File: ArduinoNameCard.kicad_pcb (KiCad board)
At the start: 2 copper layers, 91 x 55 mm, 24 parts, among them J1 Conn_01x05, J2 Conn_01x04, J3 Conn_01x06, J4 Conn_01x08, J5 Conn_01x06, SW1 SW_Push

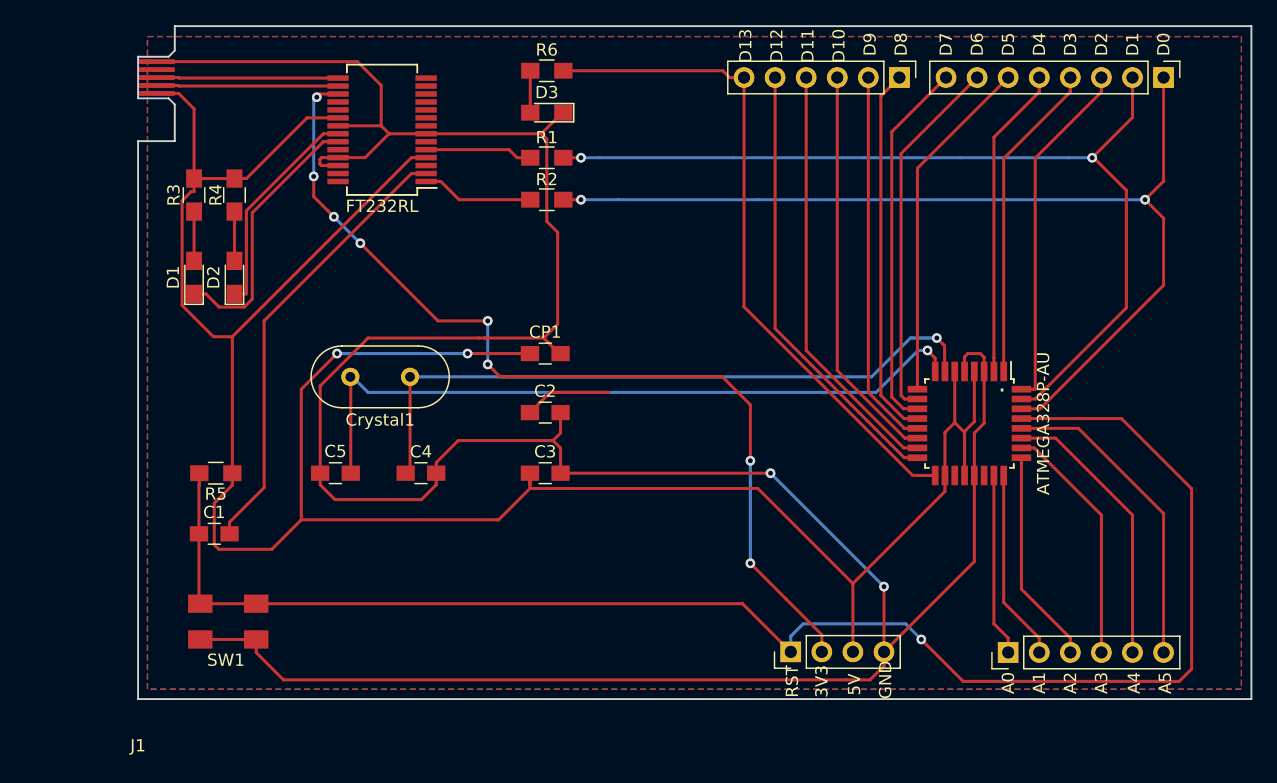
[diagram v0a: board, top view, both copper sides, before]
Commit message: ・READMEの更新 ・PCBの完成
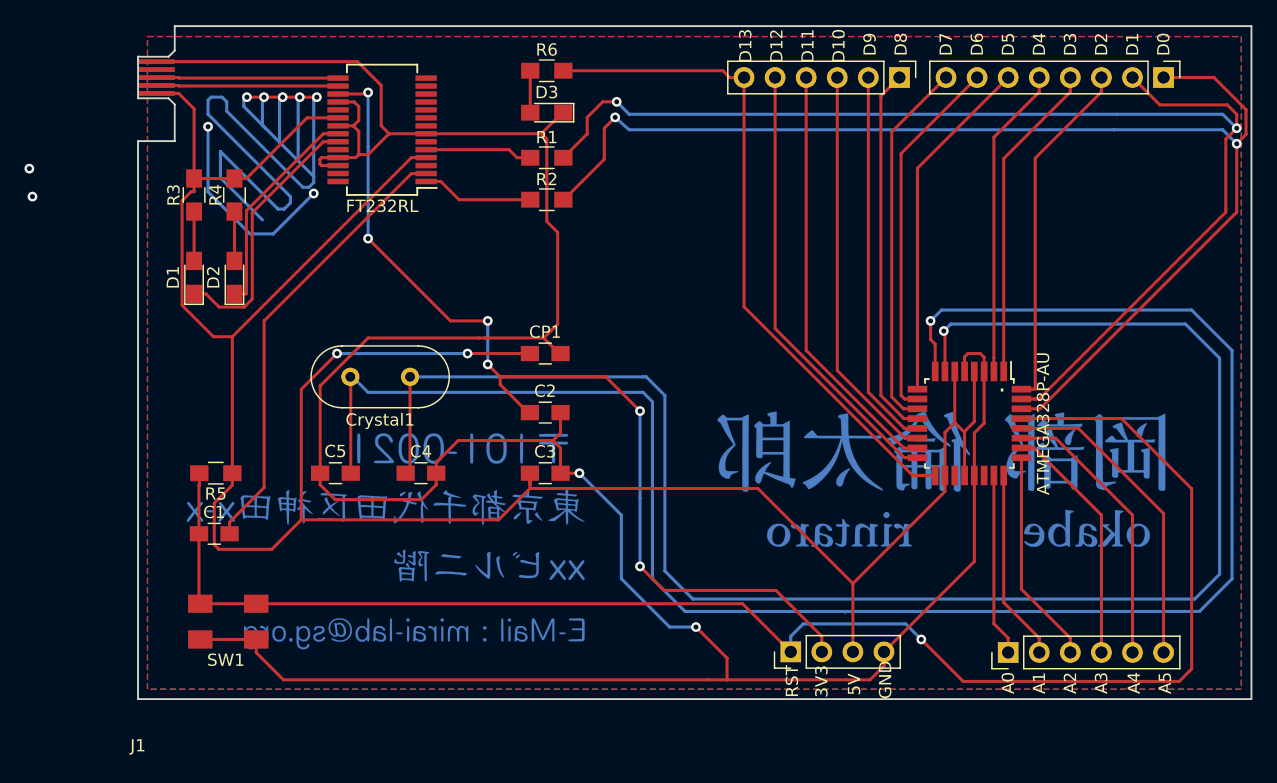
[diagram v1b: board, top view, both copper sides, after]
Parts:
- added G***: LOGO, ArduinoNameCard:belong_silk, B.Cu at (151.1, 77.0)
- added G***: LOGO, ArduinoNameCard:name_cu, B.Cu at (161.3, 99.7)
- added G***: LOGO, ArduinoNameCard:name_mask, B.Cu at (161.3, 99.7)
- added G***: LOGO, ArduinoNameCard:address_cu, B.Cu at (115.6, 104.4)
- added G***: LOGO, ArduinoNameCard:address_mask, B.Cu at (115.6, 104.4)
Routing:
- net (no net): track 0.00 -> 88.8 mm, vias 0 -> 9
- net Net-(C5-Pad1): track 59.3 -> 147.3 mm
- net Net-(C4-Pad1): track 55.4 -> 136.0 mm
- net RX: track 76.3 -> 100.0 mm
- net TX: track 81.6 -> 100.9 mm
- net GND: track 252.3 -> 245.3 mm
- net 3.3V: track 84.6 -> 79.8 mm, vias 8 -> 6

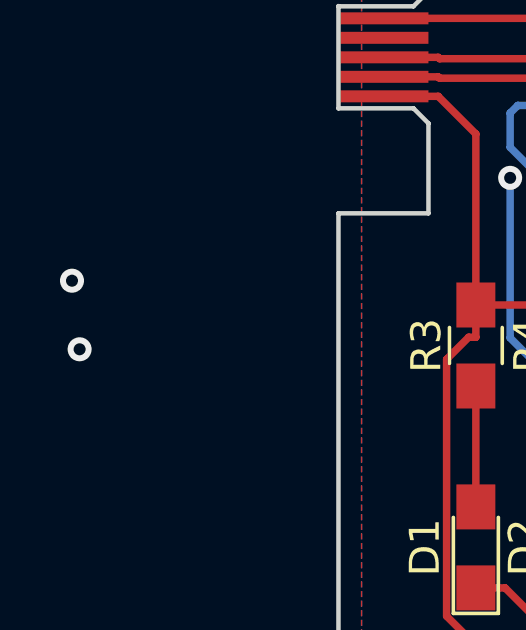
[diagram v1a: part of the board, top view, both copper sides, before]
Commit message: ・枠外にviaが残っていたので削除 ・回路図のpdfを追加
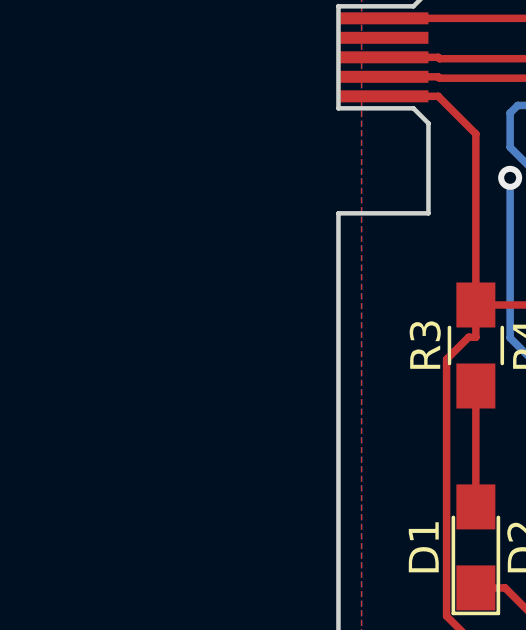
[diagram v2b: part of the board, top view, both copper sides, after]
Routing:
- net (no net): vias 9 -> 7
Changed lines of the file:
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@@
     (links 73)
     (no_connects 0)
-    (area 85.867999 61.21238 187.025001 121.645)
+    (area 91.002381 61.21238 187.025001 121.645)
     (thickness 1.6)
     (drawings 37)
-    (tracks 408)
+    (tracks 406)
     (zones 0)
     (modules 29)
@@
     (pcbplotparams
       (layerselection 0x010f0_80000001)
-      (usegerberextensions true)
+      (usegerberextensions false)
       (excludeedgelayer true)
       (linewidth 0.100000)
@@
       (plotinvisibletext false)
       (padsonsilk false)
-      (subtractmaskfromsilk true)
-      (outputformat 1)
+      (subtractmaskfromsilk false)
+      (outputformat 4)
       (mirror false)
       (drillshape 0)
@@
   (gr_line (start 95.75 64.25) (end 95.75 67.66) (angle 90) (layer Edge.Cuts) (width 0.15))
   (via (at 101.473 69.977) (size 0.8) (drill 0.4) (layers F.Cu B.Cu) (net 0))
-  (via (at 87.122 75.692) (size 0.8) (drill 0.4) (layers F.Cu B.Cu) (net 0))
-  (via (at 86.868 73.406) (size 0.8) (drill 0.4) (layers F.Cu B.Cu) (net 0))
   (via (at 110.109 75.438) (size 0.8) (drill 0.4) (layers F.Cu B.Cu) (net 0))
   (segment (start 101.473 69.977) (end 101.473 75.311) (width 0.25) (layer B.Cu) (net 0))

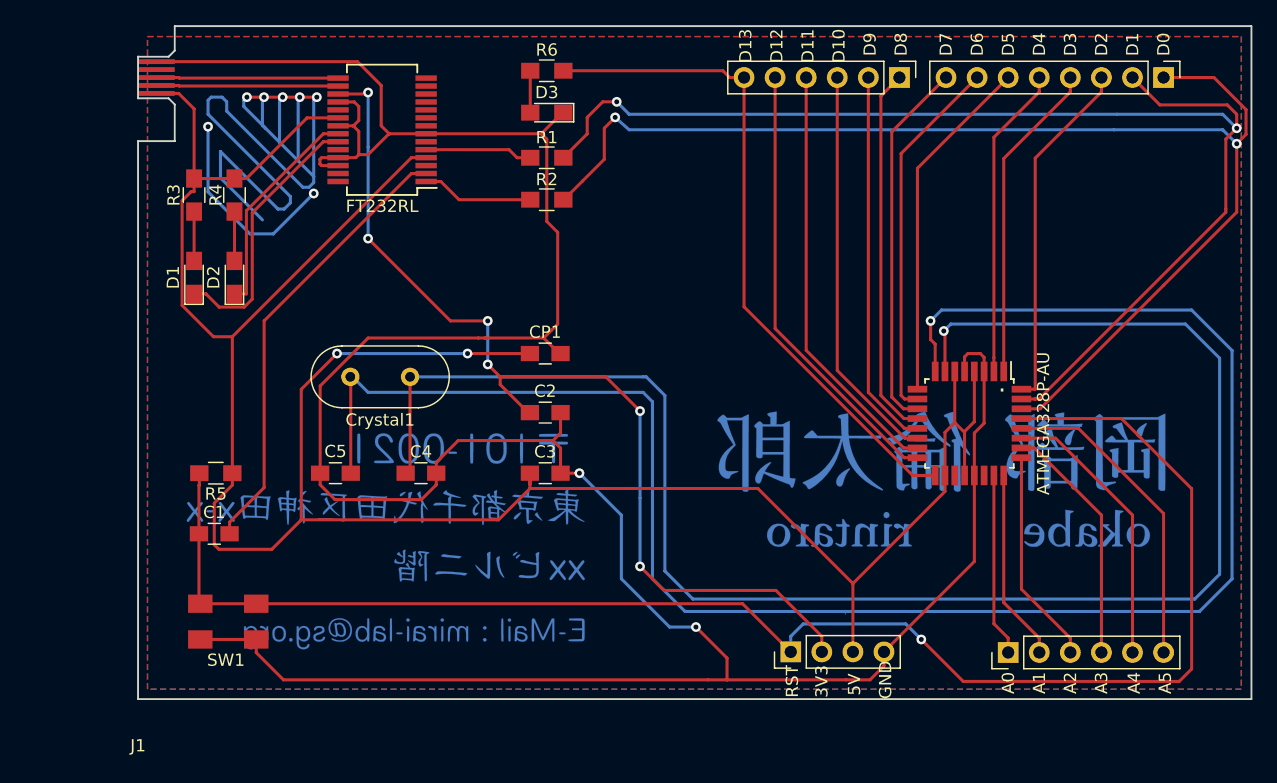
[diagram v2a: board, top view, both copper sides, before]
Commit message: 回路にヒューズを追加した
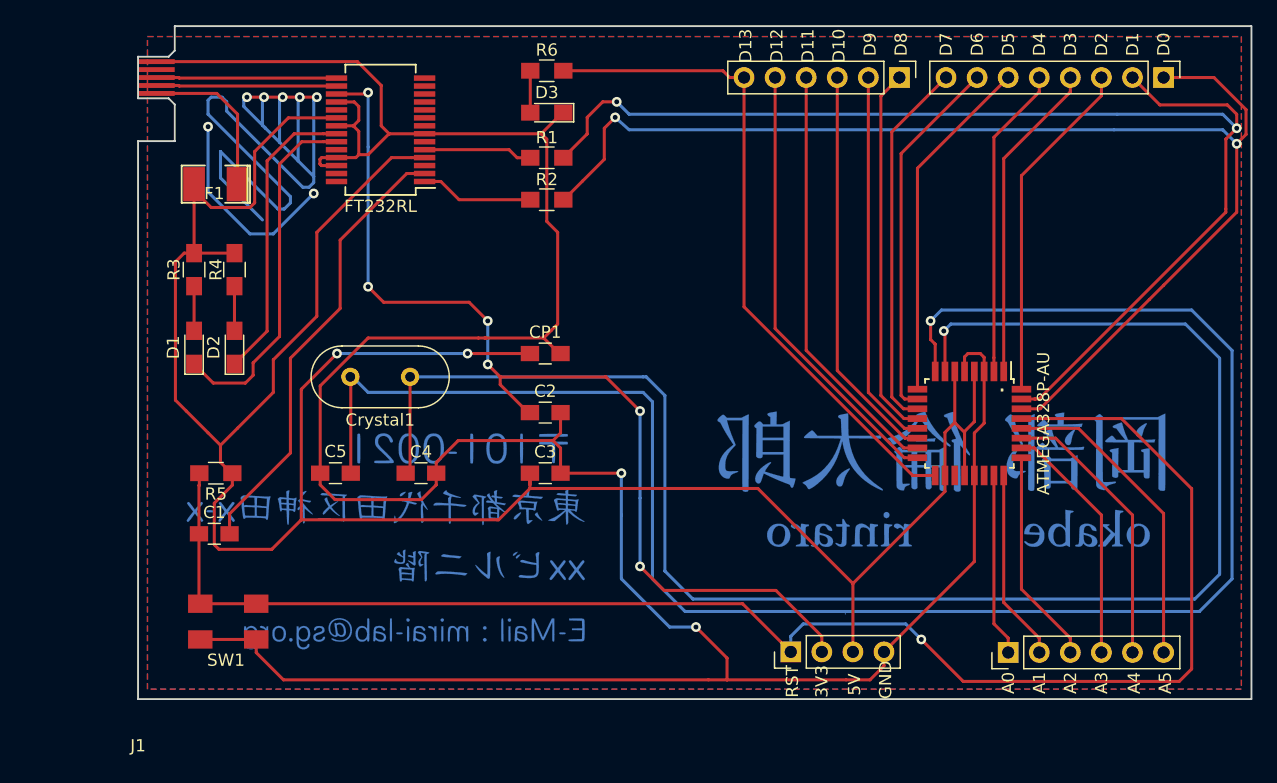
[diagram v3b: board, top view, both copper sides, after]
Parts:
- added F1: 500mA, SMD_Packages:SMD-1210_Pol, F.Cu at (102.1, 74.7)
- moved R3 6.10 mm to (100.3, 81.7)
- moved R4 6.10 mm to (103.6, 81.7)
- moved D1 5.71 mm to (100.3, 88.0)
- moved D2 5.71 mm to (103.6, 88.0)
- moved FT232RL 0.13 mm to (115.6, 70.2)
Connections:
- ATMEGA328P-AU pad 18: +5V -> 5V
- ATMEGA328P-AU pad 20: +5V -> 5V
- ATMEGA328P-AU pad 4: +5V -> 5V
- ATMEGA328P-AU pad 6: +5V -> 5V
- C3 pad 1: +5V -> 5V
- CP1 pad 1: +5V -> 5V
- FT232RL pad 20: +5V -> 5V
- FT232RL pad 4: +5V -> 5V
- J2 pad 3: +5V -> 5V
- R3 pad 1: +5V -> 5V
- R4 pad 1: +5V -> 5V
- R5 pad 1: +5V -> 5V
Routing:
- net 5V: track 0.00 -> 213.7 mm, vias 0 -> 2
- net +5V: track 205.6 -> 13.1 mm, vias 2 -> 0
- net Net-(D1-Pad1): track 21.9 -> 29.4 mm
- net Net-(D2-Pad1): track 17.9 -> 24.4 mm
- net 3.3V: track 79.8 -> 82.1 mm
- net GND: track 245.3 -> 247.3 mm
- net Net-(J4-Pad3): track 28.8 -> 28.2 mm

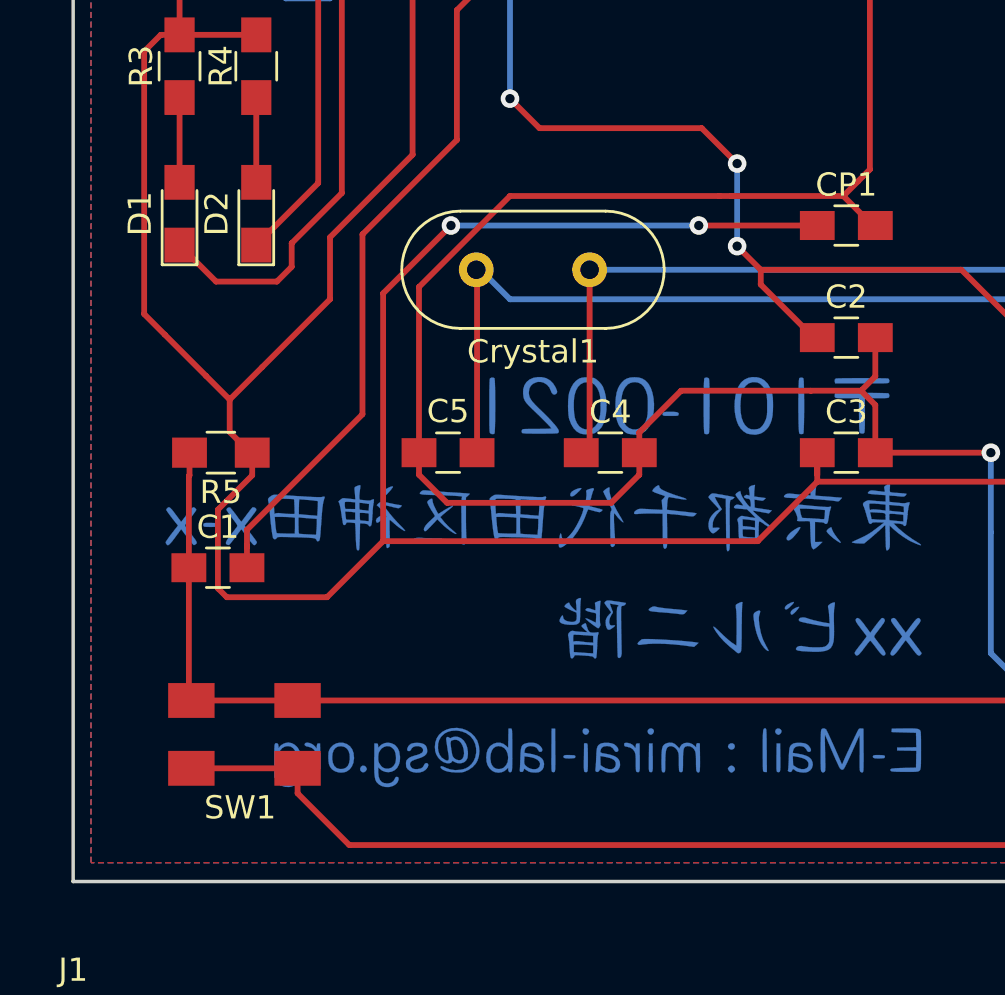
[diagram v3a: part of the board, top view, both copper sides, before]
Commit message: LEDの種類に関する追記 部品のパラメータのシルクの追加
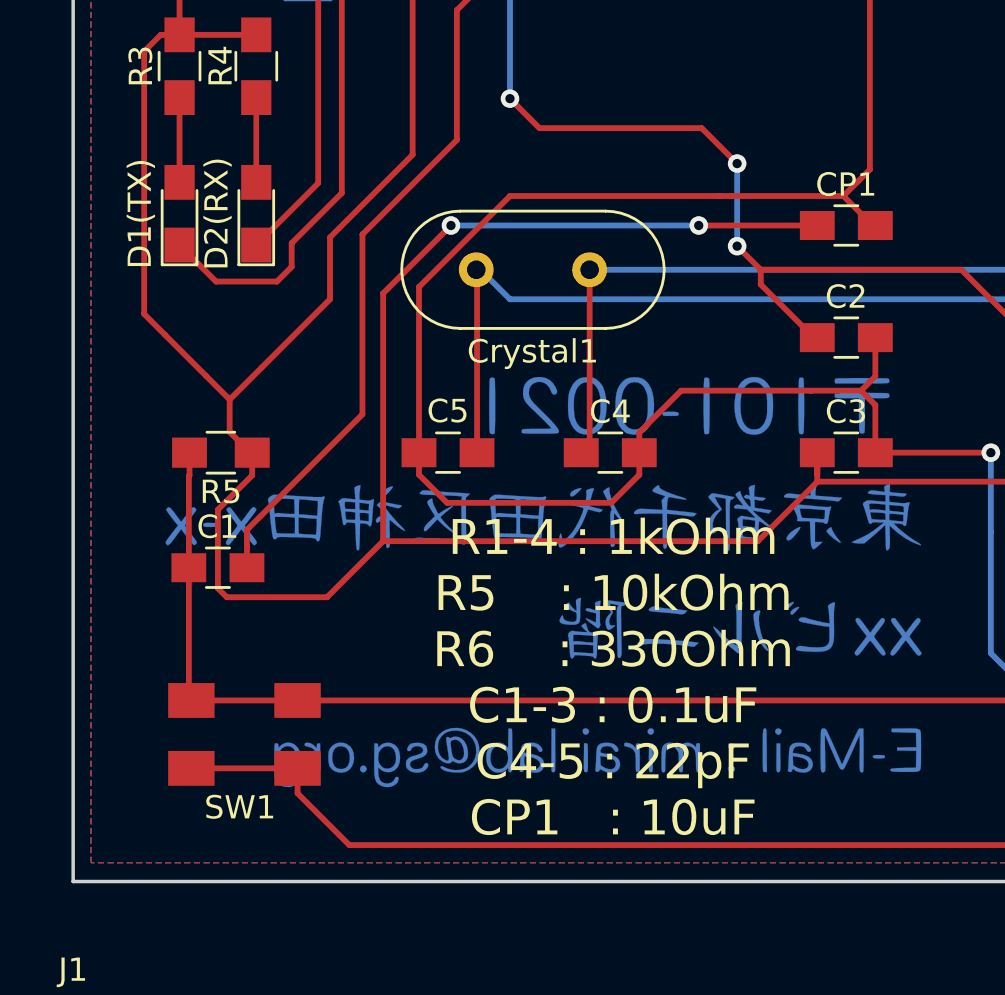
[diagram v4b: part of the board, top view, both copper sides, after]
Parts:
- D1(TX): renamed from D1; value LED -> RED
- D2(RX): renamed from D2; value LED -> GREEN
- D3: value LED -> RED
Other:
- board text added: "R1-4 : 1kOhm R5 : 10kOhm R6 : 330Ohm C1-3 : 0.1uF C4-5 : 22pF CP1 : 10uF"
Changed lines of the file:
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@@
     (links 74)
     (no_connects 0)
-    (area 95.674999 61.684999 186.825001 116.835001)
+    (area 91.002381 61.21238 187.025001 121.645)
     (thickness 1.6)
-    (drawings 37)
+    (drawings 38)
     (tracks 427)
     (zones 0)
@@
     (tags "resistor 0805")
     (attr smd)
-    (fp_text reference D1 (at 0 -1.7 90) (layer F.SilkS)
+    (fp_text reference "D1(TX)" (at 0 -1.7 90) (layer F.SilkS)
       (effects (font (size 1 1) (thickness 0.15)))
     )
-    (fp_text value LED (at 0 1.75 90) (layer F.Fab) hide
+    (fp_text value RED (at 0 1.75 90) (layer F.Fab) hide
       (effects (font (size 1 1) (thickness 0.15)))
     )
@@
     (tags "resistor 0805")
     (attr smd)
-    (fp_text reference D2 (at 0 -1.7 90) (layer F.SilkS)
+    (fp_text reference "D2(RX)" (at 0 -1.7 90) (layer F.SilkS)
       (effects (font (size 1 1) (thickness 0.15)))
     )
-    (fp_text value LED (at 0 1.75 90) (layer F.Fab) hide
+    (fp_text value GREEN (at 0 1.75 90) (layer F.Fab) hide
       (effects (font (size 1 1) (thickness 0.15)))
     )
@@
       (effects (font (size 1 1) (thickness 0.15)))
     )
-    (fp_text value LED (at -3.81 -0.127 180) (layer F.Fab)
+    (fp_text value RED (at -3.81 -0.127 180) (layer F.Fab)
       (effects (font (size 1 1) (thickness 0.15)))
     )
@@
     )
   )
+  (gr_text "R1-4 : 1kOhm\nR5    : 10kOhm\nR6    : 330Ohm\nC1-3 : 0.1uF\nC4-5 : 22pF\nCP1   : 10uF" (at 119 108) (layer F.SilkS)
+    (effects (font (size 1.5 1.5) (thickness 0.3)))
+  )
   (gr_text D13 (at 145.415 63.373 90) (layer F.SilkS)

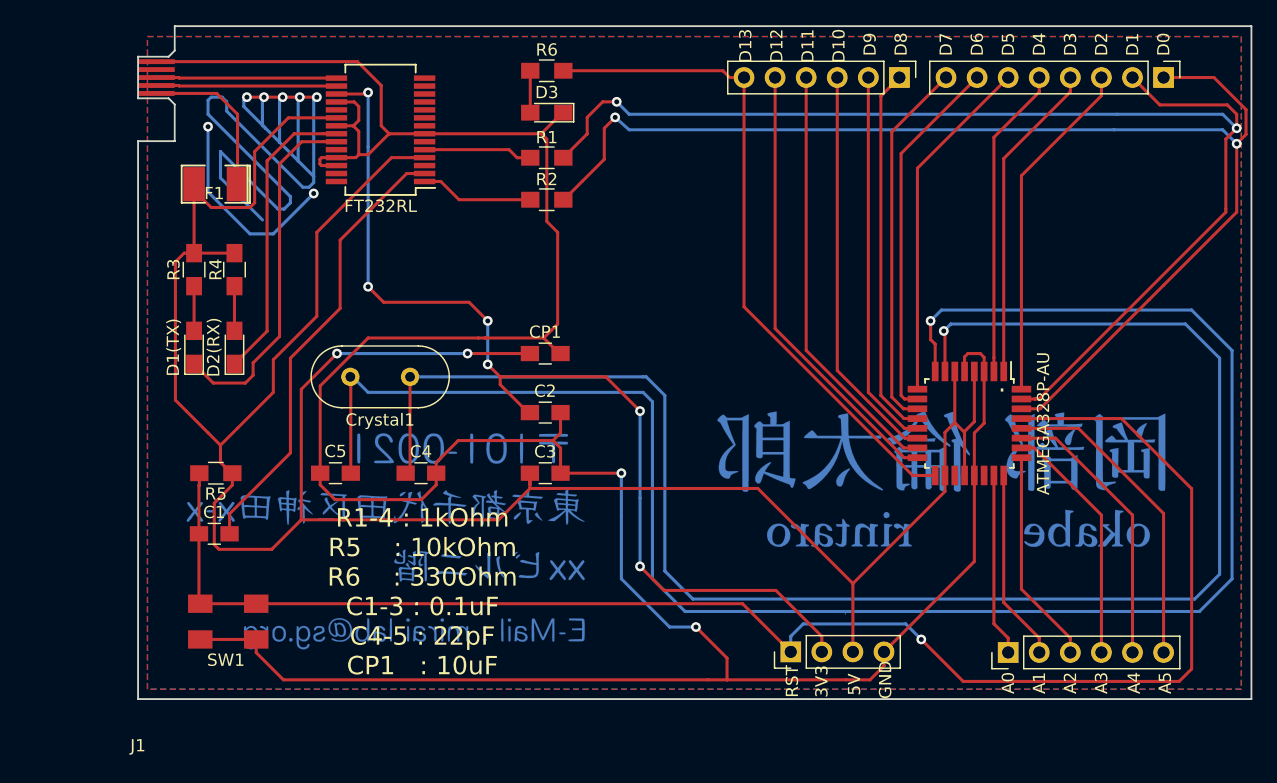
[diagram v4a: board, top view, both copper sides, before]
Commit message: 電源配線幅を拡張した
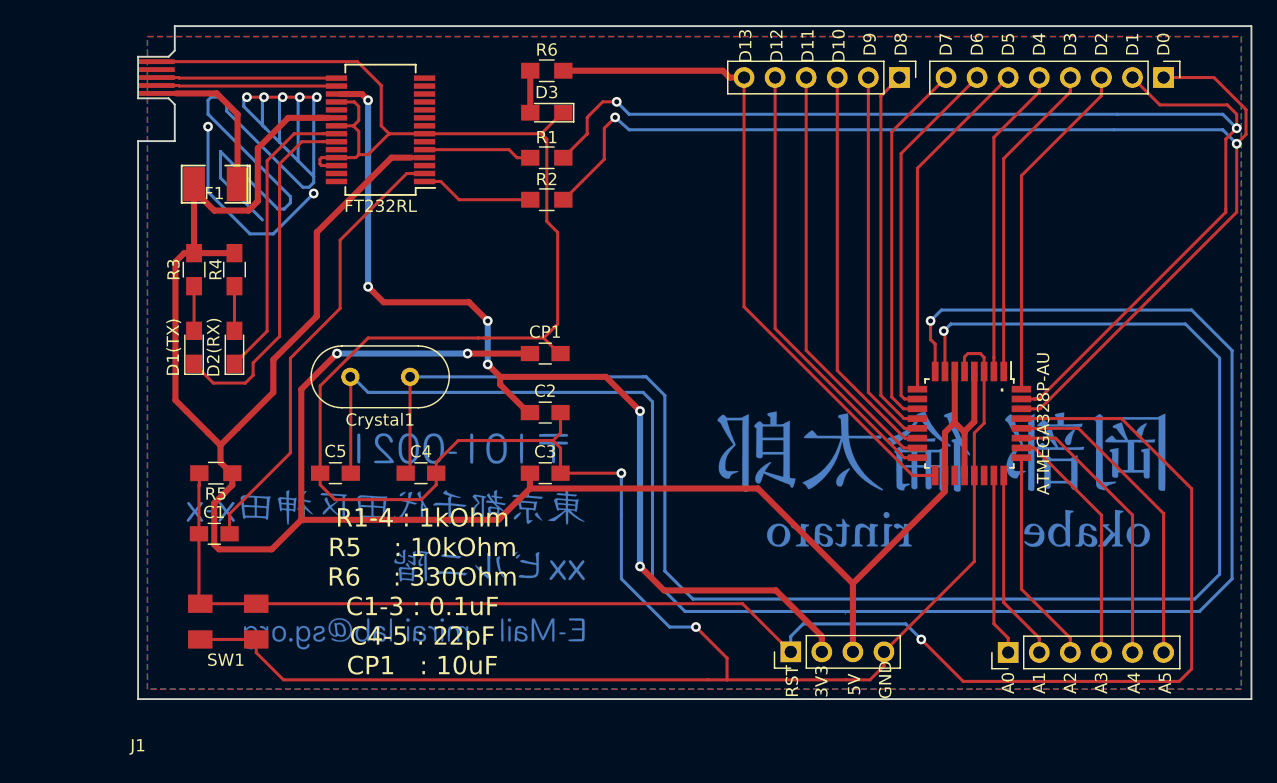
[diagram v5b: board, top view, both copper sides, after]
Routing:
- net 5V: track 213.7 -> 214.9 mm
- net 3.3V: track 82.1 -> 81.5 mm
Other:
- net class Default: trace_width 0.25 -> 0.5
